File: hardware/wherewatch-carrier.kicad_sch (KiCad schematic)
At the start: 32 parts, among them J1 LiPo JST PH, J3 u.FL GNSS antenna, J4 vibration motor, J5 speaker 4R, J6 OLED 0.42in I2C, Q1 AO3401A, Q2 2N7002, Q3 2N7002, SW1 MSK-12C02, SW2 TS-1187A, U1 XIAO ESP32S3 Sense, U2 LSM6DS3TR-C, U3 ATGM336H-5N31, U4 MAX98357A

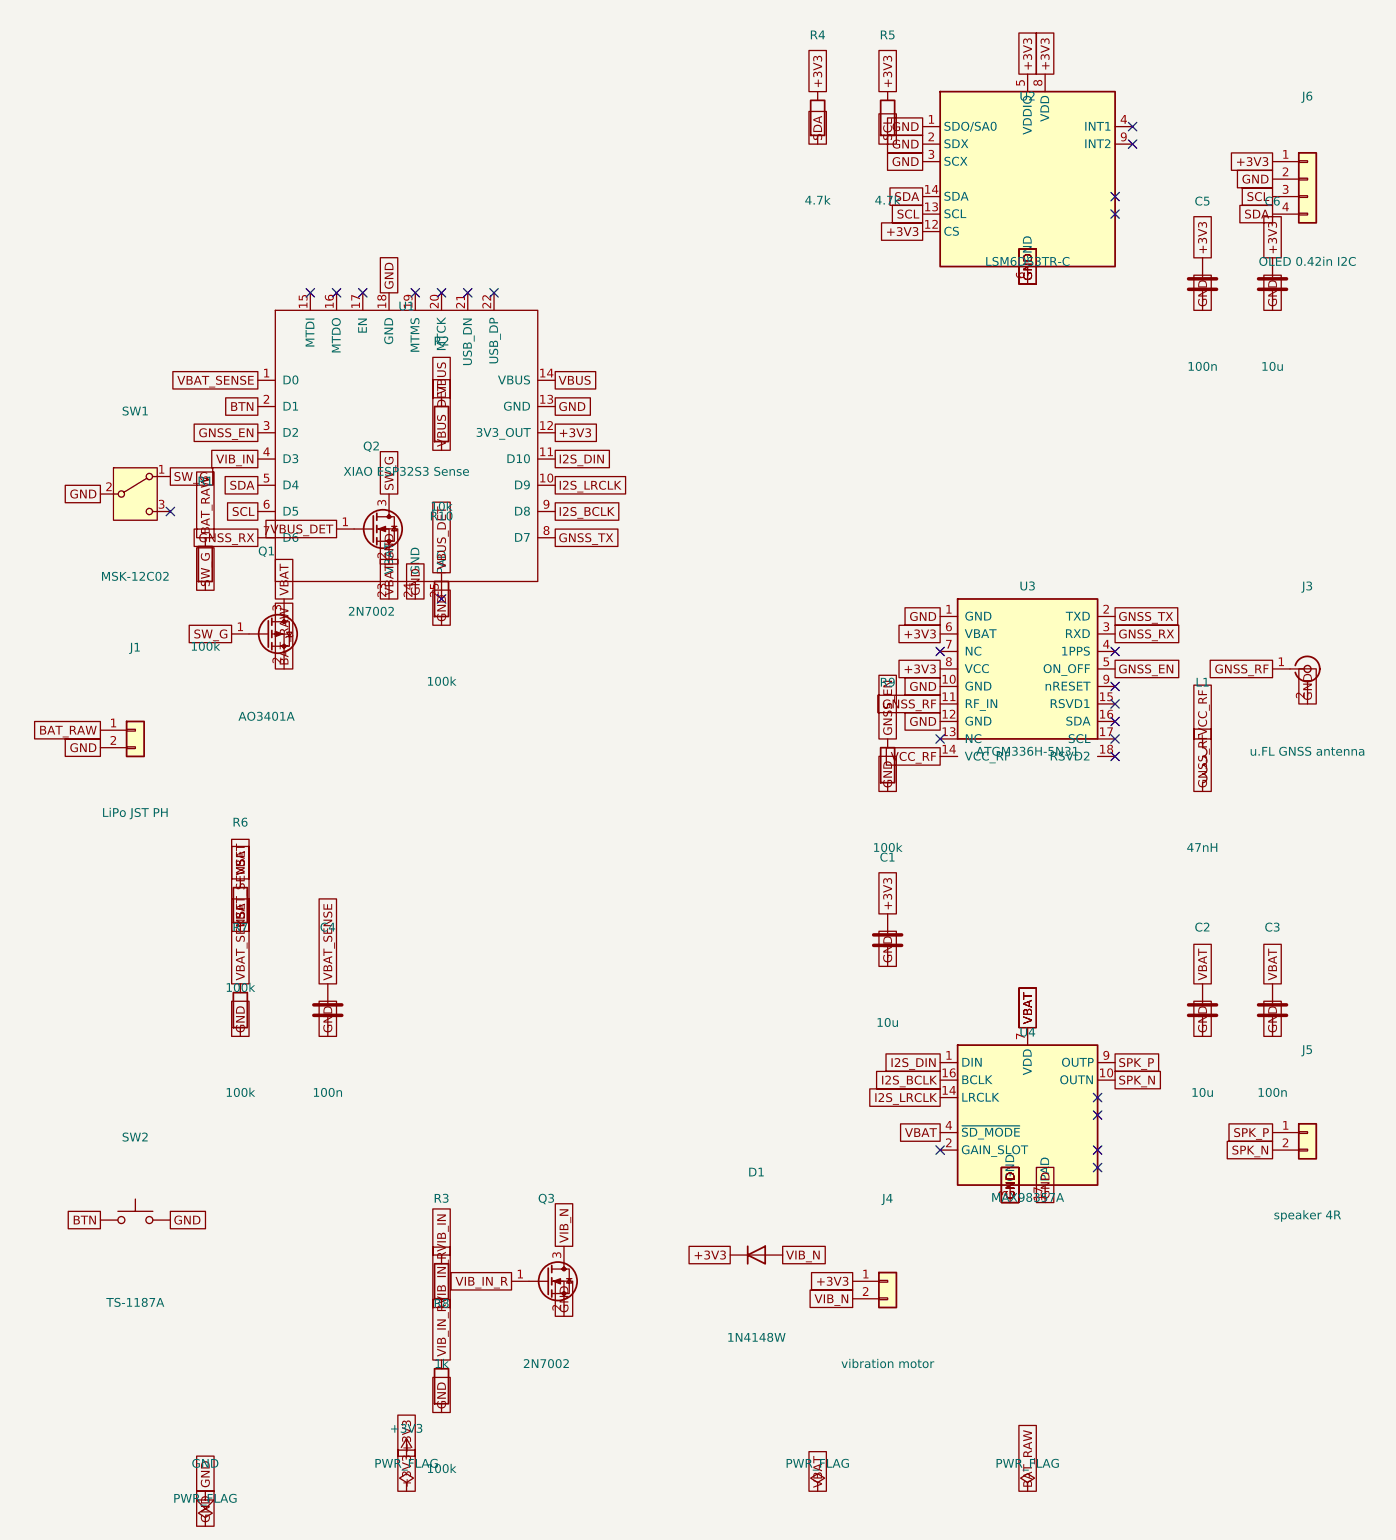
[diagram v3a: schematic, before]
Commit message: hardware: v0.3.1, AO3400A motor FET, IMU INT1 wired-OR wake, 1 M gate pull-up
codexmb's remaining P2s and claudeMB's notes: Q3 becomes AO3400A
(RDS(on) specified at 2.5 V gate drive, 5.8 A); LSM6DS3 INT1 joins the
button line with a 100 k pull-up, IMU open-drain active-low in firmware,
so motion can wake the ESP32 without a spare XIAO pin; R1 1 M cuts the
on-state gate current to 4 uA; title block v0.3; README power budget and
no-cell note. Pin order 1 G, 2 S, 3 D confirmed for both AOS parts.

Co-Authored-By: Claude Fable 5.1 <noreply@anthropic.com>
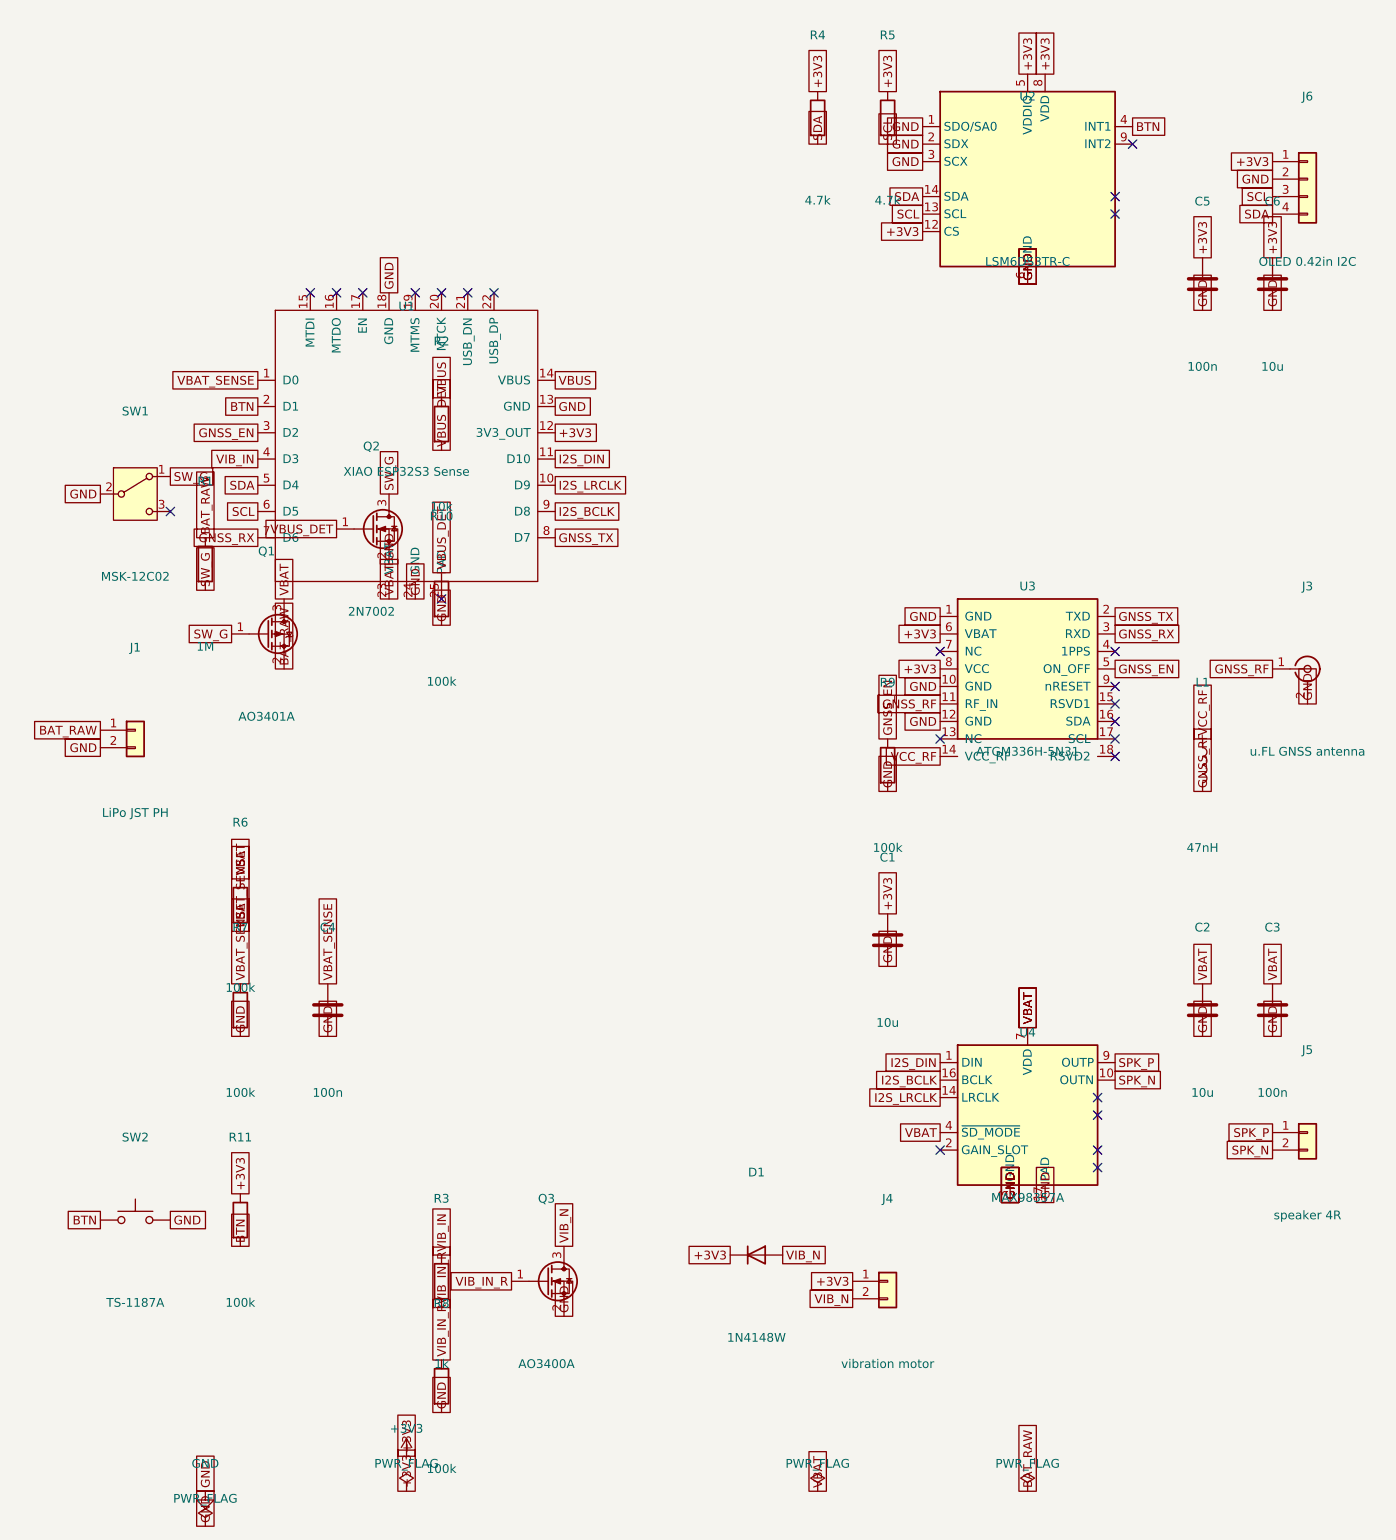
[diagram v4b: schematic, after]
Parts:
- removed Q3: 2N7002, Package_TO_SOT_SMD:SOT-23, symbol Transistor_FET:2N7002
- added Q3: AO3400A, Package_TO_SOT_SMD:SOT-23, symbol Transistor_FET:AO3400A
- added R11: 100k, Resistor_SMD:R_0402_1005Metric, symbol Device:R
- R1: value 100k -> 1M
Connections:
- net +3V3: now also R11.1
- net BTN: now also U2.4 (INT1), R11.2
- net GND: now also Q3.2 (S)
- net VIB_IN_R: now also Q3.1 (G)
- net VIB_N: now also Q3.3 (D)
- no-connect marks 26 -> 25
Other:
- title: WhereWatch carrier PCB v0 -> WhereWatch carrier PCB v0.3
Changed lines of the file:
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@@
 (kicad_sch (version 20250114) (generator "gen_schematic.py") (generator_version "10.0")
   (paper "A3")
-  (title_block (title "WhereWatch carrier PCB v0") (date "2026-09-09") (rev "v0") (company "ThinkOff") (comment 1 "generated by hardware/gen_schematic.py; connectivity by global labels; see hardware/README.md"))
+  (title_block (title "WhereWatch carrier PCB v0.3") (date "2026-09-09") (rev "v0.3") (company "ThinkOff") (comment 1 "generated by hardware/gen_schematic.py; connectivity by global labels; see hardware/README.md"))
   (symbol (lib_id "Seeed_XIAO:XIAO-ESP32-S3-SMD") (at 59.69 69.85 0) (unit 1) (exclude_from_sim no) (in_bom yes) (on_board yes) (dnp no)
     (property "Reference" "U1" (at 59.69 57.85 0) (effects (font (size 1.27 1.27))))
@@
     (property "Datasheet" "" (at 190.50 110.49 0) (effects (font (size 1.27 1.27)) (hide yes)))
     (instances (project "wherewatch-carrier" (path "/7b0b4b2e-2c0d-4f5e-9a6a-000000000001" (reference "J3") (unit 1)))))
-  (symbol (lib_id "Transistor_FET:2N7002") (at 80.01 199.39 0) (unit 1) (exclude_from_sim no) (in_bom yes) (on_board yes) (dnp no)
+  (symbol (lib_id "Transistor_FET:AO3400A") (at 80.01 199.39 0) (unit 1) (exclude_from_sim no) (in_bom yes) (on_board yes) (dnp no)
     (property "Reference" "Q3" (at 80.01 187.39 0) (effects (font (size 1.27 1.27))))
-    (property "Value" "2N7002" (at 80.01 211.39 0) (effects (font (size 1.27 1.27))))
+    (property "Value" "AO3400A" (at 80.01 211.39 0) (effects (font (size 1.27 1.27))))
     (property "Footprint" "Package_TO_SOT_SMD:SOT-23" (at 80.01 199.39 0) (effects (font (size 1.27 1.27)) (hide yes)))
     (property "Datasheet" "" (at 80.01 199.39 0) (effects (font (size 1.27 1.27)) (hide yes)))
-    (property "LCSC" "C8545" (at 80.01 199.39 0) (effects (font (size 1.27 1.27)) (hide yes)))
+    (property "LCSC" "C20917" (at 80.01 199.39 0) (effects (font (size 1.27 1.27)) (hide yes)))
     (instances (project "wherewatch-carrier" (path "/7b0b4b2e-2c0d-4f5e-9a6a-000000000001" (reference "Q3") (unit 1)))))
   (symbol (lib_id "Device:R") (at 64.77 199.39 0) (unit 1) (exclude_from_sim no) (in_bom yes) (on_board yes) (dnp no)
@@
   (symbol (lib_id "Device:R") (at 30.48 95.25 0) (unit 1) (exclude_from_sim no) (in_bom yes) (on_board yes) (dnp no)
     (property "Reference" "R1" (at 30.48 83.25 0) (effects (font (size 1.27 1.27))))
-    (property "Value" "100k" (at 30.48 107.25 0) (effects (font (size 1.27 1.27))))
+    (property "Value" "1M" (at 30.48 107.25 0) (effects (font (size 1.27 1.27))))
     (property "Footprint" "Resistor_SMD:R_0402_1005Metric" (at 30.48 95.25 0) (effects (font (size 1.27 1.27)) (hide yes)))
     (property "Datasheet" "" (at 30.48 95.25 0) (effects (font (size 1.27 1.27)) (hide yes)))
@@
     (property "LCSC" "C318884" (at 20.32 190.50 0) (effects (font (size 1.27 1.27)) (hide yes)))
     (instances (project "wherewatch-carrier" (path "/7b0b4b2e-2c0d-4f5e-9a6a-000000000001" (reference "SW2") (unit 1)))))
+  (symbol (lib_id "Device:R") (at 35.56 190.50 0) (unit 1) (exclude_from_sim no) (in_bom yes) (on_board yes) (dnp no)
+    (property "Reference" "R11" (at 35.56 178.50 0) (effects (font (size 1.27 1.27))))
+    (property "Value" "100k" (at 35.56 202.50 0) (effects (font (size 1.27 1.27))))
+    (property "Footprint" "Resistor_SMD:R_0402_1005Metric" (at 35.56 190.50 0) (effects (font (size 1.27 1.27)) (hide yes)))
+    (property "Datasheet" "" (at 35.56 190.50 0) (effects (font (size 1.27 1.27)) (hide yes)))
+    (instances (project "wherewatch-carrier" (path "/7b0b4b2e-2c0d-4f5e-9a6a-000000000001" (reference "R11") (unit 1)))))
   (symbol (lib_id "Device:C") (at 175.26 54.61 0) (unit 1) (exclude_from_sim no) (in_bom yes) (on_board yes) (dnp no)
     (property "Reference" "C5" (at 175.26 42.61 0) (effects (font (size 1.27 1.27))))
@@
     (effects (font (size 1.27 1.27)) (justify right))
     (property "Intersheetrefs" "${INTERSHEET_REFS}" (at 134.62 41.91 0) (effects (font (size 1.27 1.27)) (hide yes))))
+  (global_label "BTN" (shape passive) (at 165.10 31.75 0) (fields_autoplaced yes)
+    (effects (font (size 1.27 1.27)) (justify left))
+    (property "Intersheetrefs" "${INTERSHEET_REFS}" (at 165.10 31.75 0) (effects (font (size 1.27 1.27)) (hide yes))))
   (global_label "GND" (shape passive) (at 137.16 102.87 180) (fields_autoplaced yes)
     (effects (font (size 1.27 1.27)) (justify right))
@@
     (effects (font (size 1.27 1.27)) (justify left))
     (property "Intersheetrefs" "${INTERSHEET_REFS}" (at 25.40 190.50 0) (effects (font (size 1.27 1.27)) (hide yes))))
+  (global_label "+3V3" (shape passive) (at 35.56 186.69 90) (fields_autoplaced yes)
+    (effects (font (size 1.27 1.27)) (justify left))
+    (property "Intersheetrefs" "${INTERSHEET_REFS}" (at 35.56 186.69 0) (effects (font (size 1.27 1.27)) (hide yes))))
+  (global_label "BTN" (shape passive) (at 35.56 194.31 270) (fields_autoplaced yes)
+    (effects (font (size 1.27 1.27)) (justify left))
+    (property "Intersheetrefs" "${INTERSHEET_REFS}" (at 35.56 194.31 0) (effects (font (size 1.27 1.27)) (hide yes))))
   (global_label "+3V3" (shape passive) (at 175.26 50.80 90) (fields_autoplaced yes)
     (effects (font (size 1.27 1.27)) (justify left))
@@
     (effects (font (size 1.27 1.27)) (justify left))
 )
+  (no_connect (at 53.34 55.88))
+  (no_connect (at 49.53 55.88))
+  (no_connect (at 64.77 100.33))
+  (no_connect (at 64.77 55.88))
+  (no_connect (at 45.72 55.88))
   (no_connect (at 60.96 55.88))
+  (no_connect (at 72.39 55.88))
   (no_connect (at 68.58 55.88))
-  (no_connect (at 64.77 100.33))
-  (no_connect (at 53.34 55.88))
-  (no_connect (at 45.72 55.88))
-  (no_connect (at 64.77 55.88))
-  (no_connect (at 49.53 55.88))
-  (no_connect (at 72.39 55.88))
-  (no_connect (at 162.56 44.45))
   (no_connect (at 165.10 34.29))
   (no_connect (at 162.56 41.91))
-  (no_connect (at 165.10 31.75))
-  (no_connect (at 137.16 120.65))
+  (no_connect (at 162.56 44.45))
   (no_connect (at 162.56 120.65))
+  (no_connect (at 162.56 118.11))
   (no_connect (at 162.56 115.57))
   (no_connect (at 137.16 107.95))
+  (no_connect (at 162.56 107.95))
+  (no_connect (at 137.16 120.65))
   (no_connect (at 162.56 123.19))
-  (no_connect (at 162.56 118.11))
   (no_connect (at 162.56 113.03))
-  (no_connect (at 162.56 107.95))
+  (no_connect (at 137.16 180.34))
+  (no_connect (at 160.02 180.34))
   (no_connect (at 160.02 172.72))
   (no_connect (at 160.02 182.88))
   (no_connect (at 160.02 175.26))
-  (no_connect (at 160.02 180.34))
-  (no_connect (at 137.16 180.34))
   (no_connect (at 25.40 87.63))
   (sheet_instances (path "/" (page "1")))
